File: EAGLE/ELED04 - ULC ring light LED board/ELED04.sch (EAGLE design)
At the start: 39 parts, among them J7 RINGLIGHT

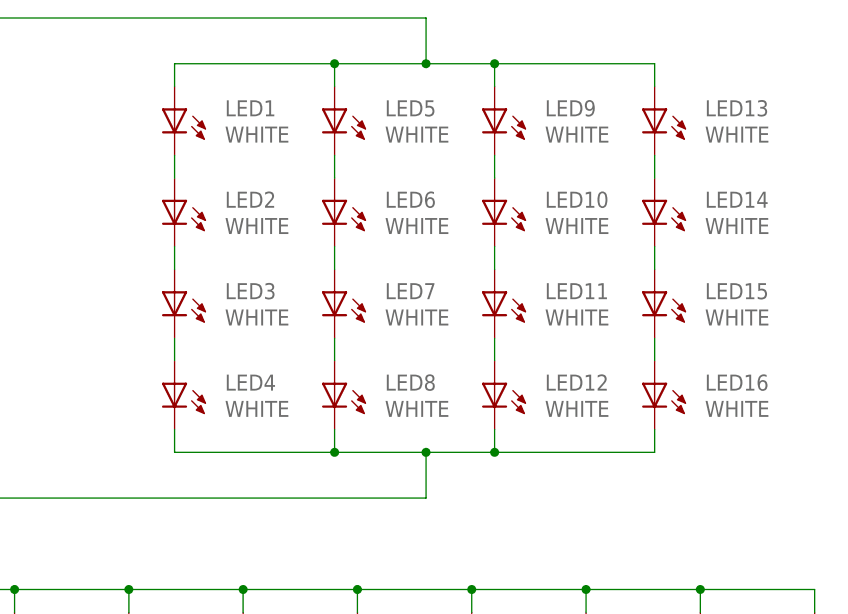
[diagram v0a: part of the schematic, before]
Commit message: On the two ring light boards, I changed the LEDs from 1206 package to 1210 in order to accomodate a brighter LED.
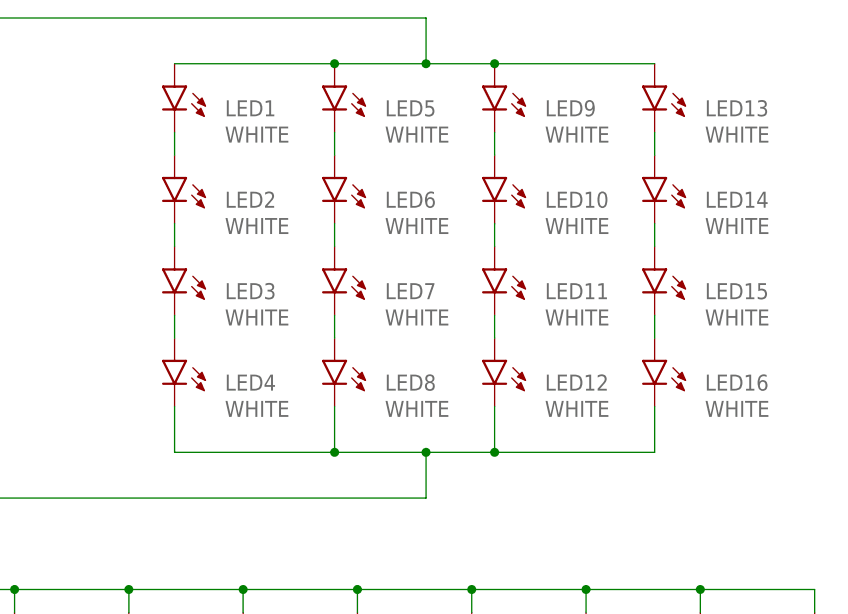
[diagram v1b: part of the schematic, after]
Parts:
- LED1, LED10, LED11, LED12, LED13, LED14, LED15, LED16, LED2, LED3, LED4, LED5, LED6, LED7, LED8, LED9: device SparkFun-LED:LED1206-NS -> GinWhiskers - temp stuff:LED1210

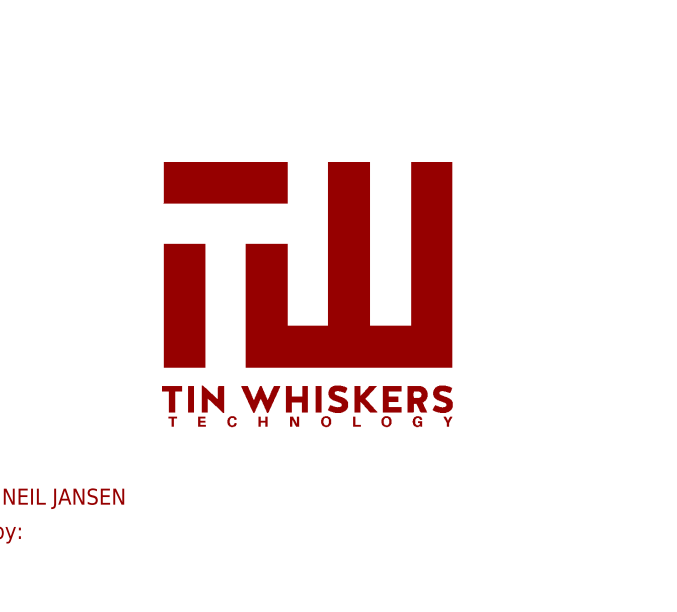
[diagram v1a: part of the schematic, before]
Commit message: Added frames, logos, part numbers, and fiducials
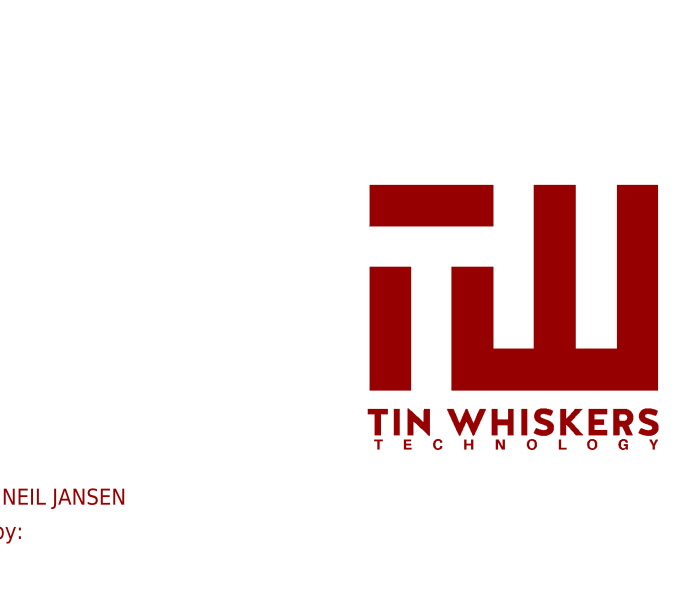
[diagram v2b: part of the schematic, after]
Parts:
- removed U$1: TIN-WHISKERSSMALL, !tin-whiskers:TIN-WHISKERSSMALL
- added U$3: TIN-WHISKERSSMALL, !tin-whiskers-logo:TIN-WHISKERSSMALL
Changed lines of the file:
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@@
 <attribute name="PARTNO" value="LTST-C150CKT"/>
 </part>
-<part name="U$1" library="!tin-whiskers" deviceset="TIN-WHISKERS" device="SMALL"/>
 <part name="J7" library="TinWhiskers" deviceset="CPL-CON-JST-2.0MM-5P-SMT-VRT" device="" value="RINGLIGHT"/>
 <part name="LED17" library="GinWhiskers - temp stuff" deviceset="WS2812B" device=""/>
@@
 <part name="C8" library="TinWhiskers" deviceset="CPL-CAP-X5R-0603-0.1UF-35V" device="" value="0.1uF"/>
 <part name="C9" library="TinWhiskers" deviceset="CPL-CAP-X5R-0603-0.1UF-35V" device="" value="0.1uF"/>
+<part name="U$3" library="!tin-whiskers-logo" deviceset="TIN-WHISKERS" device="SMALL"/>
 </parts>
 <sheets>
@@
 <attribute name="PARTNO" x="193.04" y="129.54" size="1.778" layer="96" display="off"/>
 </instance>
-<instance part="U$1" gate="G$1" x="317.5" y="27.94"/>
 <instance part="J7" gate="G$1" x="86.36" y="134.62"/>
 <instance part="LED17" gate="G$1" x="121.92" y="99.06" smashed="yes">
@@
 <instance part="C8" gate="G$1" x="198.12" y="78.74" rot="R270"/>
 <instance part="C9" gate="G$1" x="210.82" y="78.74" rot="R270"/>
+<instance part="U$3" gate="G$1" x="340.36" y="25.4"/>
 </instances>
 <busses>

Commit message: Replaced fiducials with newer fiducials that have keepouts / restrict layers
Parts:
- FID1, FID2, FID3, FID4: value FIDUCIAL1X2 -> FIDUCIAL; device SparkFun-Aesthetics:FIDUCIAL1X2 -> TinWhiskers:FIDUCIAL
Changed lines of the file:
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@@
 <attribute name="PARTNO" value="LTST-C150CKT"/>
 </part>
-<part name="FID1" library="SparkFun-Aesthetics" deviceset="FIDUCIAL" device="1X2"/>
-<part name="FID2" library="SparkFun-Aesthetics" deviceset="FIDUCIAL" device="1X2"/>
-<part name="FID3" library="SparkFun-Aesthetics" deviceset="FIDUCIAL" device="1X2"/>
-<part name="FID4" library="SparkFun-Aesthetics" deviceset="FIDUCIAL" device="1X2"/>
+<part name="FID1" library="TinWhiskers" deviceset="FIDUCIAL" device=""/>
+<part name="FID2" library="TinWhiskers" deviceset="FIDUCIAL" device=""/>
+<part name="FID3" library="TinWhiskers" deviceset="FIDUCIAL" device=""/>
+<part name="FID4" library="TinWhiskers" deviceset="FIDUCIAL" device=""/>
 <part name="FRAME1" library="frames" deviceset="A3L-LOC" device=""/>
 <part name="LOGO4" library="FirePick" deviceset="LOGO-FIREPICK" device="MEDIUM" value="LOGO-FIREPICKMEDIUM">
@@
 <attribute name="PARTNO" x="175.26" y="129.54" size="1.778" layer="96" display="off"/>
 </instance>
-<instance part="FID1" gate="G$1" x="279.4" y="12.7"/>
-<instance part="FID2" gate="G$1" x="279.4" y="7.62"/>
-<instance part="FID3" gate="G$1" x="284.48" y="12.7"/>
+<instance part="FID1" gate="G$1" x="276.86" y="15.24"/>
+<instance part="FID2" gate="G$1" x="276.86" y="7.62"/>
+<instance part="FID3" gate="G$1" x="284.48" y="15.24"/>
 <instance part="FID4" gate="G$1" x="284.48" y="7.62"/>
 <instance part="FRAME1" gate="G$1" x="0.000003125" y="0"/>

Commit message: Created ESOL01 Schematic and Board. Added parts to DB, added parts to inventory.
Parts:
- C2, C3, C4, C5, C6, C7, C8, C9: PARTNO (none) -> GMK107BJ104KAHT
- FID1, FID2, FID3, FID4, U$3: PARTNO (none) -> *
- J7: PARTNO (none) -> B5B-PH-SM4-TB(LF)(SN)
- LED1, LED10, LED11, LED12, LED13, LED14, LED15, LED16, LED2, LED3, LED4, LED5, LED6, LED7, LED8, LED9: PARTNO LTST-C150CKT -> QBLP650-IW
- LED17, LED18, LED19, LED20, LED21, LED22, LED23, LED24: PARTNO (none) -> 1655
